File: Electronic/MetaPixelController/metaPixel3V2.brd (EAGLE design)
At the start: 100 x 80 mm, 3 parts, among them IC1 74HC245N

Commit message: fixing include stuff
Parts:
- added JP1: (no value), pinhead:1X01
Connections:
- removed net !MEM_CS: U$1.6
- removed net !SD_CS: U$1.10
- removed net A_BCLK: U$1.9
- removed net A_LRCLK: U$1.23/A9
- removed net A_MCLK: U$1.11
- removed net A_RX: U$1.13
- removed net A_TX: U$1.22/A8
- removed net SCL: U$1.19/A5
- removed net SDA: U$1.18/A4
- net !LCD_CS: now also U$1.10; no longer U$1.20/A6
- net LCD_DC: now also U$1.9; no longer U$1.15/A1
- net LCD_LED: now also JP1.1; no longer U$1.3
- net MOSI: now also U$1.11; no longer U$1.7
- net SCLK: now also U$1.13; no longer U$1.14/A0
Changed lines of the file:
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@@
 </element>
 <element name="U$1" library="Teensy3.0" package="TEENSY_3.0_BASIC" value="TEENSY_3.0_BASIC" x="25.4" y="26.67"/>
+<element name="JP1" library="pinhead" package="1X01" value="" x="2.54" y="-3.81"/>
 </elements>
 <signals>
@@
 </signal>
 <signal name="SCLK">
-<contactref element="U$1" pad="14/A0"/>
 <contactref element="SV1" pad="10"/>
 <wire x1="91.44" y1="28.3464" x2="91.44" y2="29.21" width="0.254" layer="16"/>
@@
 <wire x1="42.9768" y1="22.6314" x2="88.9254" y2="22.6314" width="0.254" layer="16"/>
 <wire x1="33.147" y1="12.8016" x2="42.9768" y2="22.6314" width="0.254" layer="16"/>
-<wire x1="33.147" y1="12.8016" x2="33.02" y2="12.7" width="0.254" layer="16"/>
-</signal>
-<signal name="A_BCLK">
-<contactref element="U$1" pad="9"/>
+<contactref element="U$1" pad="13"/>
+<wire x1="33.02" y1="10.16" x2="33.147" y2="12.8016" width="0" layer="19" extent="16-16"/>
 </signal>
 <signal name="MOSI">
-<contactref element="U$1" pad="7"/>
 <contactref element="SV1" pad="8"/>
 <wire x1="90.297" y1="31.5468" x2="91.44" y2="31.5468" width="0.254" layer="1"/>
@@
 <wire x1="17.8308" y1="22.86" x2="18.9738" y2="24.003" width="0.254" layer="1"/>
 <wire x1="91.44" y1="31.5468" x2="91.44" y2="31.75" width="0.254" layer="1"/>
-<wire x1="17.8308" y1="22.86" x2="17.78" y2="22.86" width="0.254" layer="1"/>
+<contactref element="U$1" pad="11"/>
+<wire x1="17.78" y1="12.7" x2="17.8308" y2="22.86" width="0" layer="19" extent="1-1"/>
 </signal>
 <signal name="MISO">
-<contactref element="U$1" pad="12"/>
 <contactref element="SV1" pad="9"/>
 <wire x1="57.6072" y1="29.0322" x2="88.6968" y2="29.0322" width="0.254" layer="1"/>
@@
 <wire x1="17.8308" y1="10.287" x2="24.003" y2="16.4592" width="0.254" layer="1"/>
 <wire x1="88.6968" y1="29.0322" x2="88.9" y2="29.21" width="0.254" layer="1"/>
-<wire x1="17.8308" y1="10.287" x2="17.78" y2="10.16" width="0.254" layer="1"/>
-</signal>
-<signal name="A_LRCLK">
-<contactref element="U$1" pad="23/A9"/>
-</signal>
-<signal name="A_RX">
-<contactref element="U$1" pad="13"/>
-</signal>
-<signal name="A_TX">
-<contactref element="U$1" pad="22/A8"/>
-</signal>
-<signal name="A_MCLK">
-<contactref element="U$1" pad="11"/>
-</signal>
-<signal name="!SD_CS">
-<contactref element="U$1" pad="10"/>
-</signal>
-<signal name="!MEM_CS">
-<contactref element="U$1" pad="6"/>
-</signal>
-<signal name="SCL">
-<contactref element="U$1" pad="19/A5"/>
-</signal>
-<signal name="SDA">
-<contactref element="U$1" pad="18/A4"/>
+<contactref element="U$1" pad="12"/>
+<wire x1="17.78" y1="10.16" x2="17.8308" y2="10.287" width="0" layer="19" extent="1-1"/>
 </signal>
 <signal name="LCD_LED">
 <contactref element="SV1" pad="5"/>
-<contactref element="U$1" pad="3"/>
 <wire x1="35.8902" y1="34.29" x2="88.9" y2="34.29" width="0.254" layer="1"/>
 <wire x1="33.3756" y1="36.8046" x2="35.8902" y2="34.29" width="0.254" layer="1"/>
@@
 <wire x1="16.6878" y1="34.0614" x2="16.6878" y2="36.1188" width="0.254" layer="1"/>
 <wire x1="17.6022" y1="33.147" x2="16.6878" y2="34.0614" width="0.254" layer="1"/>
-<wire x1="17.6022" y1="33.147" x2="17.78" y2="33.02" width="0.254" layer="1"/>
+<contactref element="JP1" pad="1"/>
+<wire x1="2.54" y1="-3.81" x2="17.6022" y2="33.147" width="0" layer="19" extent="1-1"/>
 </signal>
 <signal name="!LCD_CS">
 <contactref element="SV1" pad="7"/>
-<contactref element="U$1" pad="20/A6"/>
 <wire x1="85.4964" y1="31.5468" x2="88.6968" y2="31.5468" width="0.254" layer="1"/>
 <wire x1="84.8106" y1="30.861" x2="85.4964" y2="31.5468" width="0.254" layer="1"/>
@@
 <wire x1="33.147" y1="28.1178" x2="55.3212" y2="28.1178" width="0.254" layer="1"/>
 <wire x1="88.6968" y1="31.5468" x2="88.9" y2="31.75" width="0.254" layer="1"/>
-<wire x1="33.147" y1="28.1178" x2="33.02" y2="27.94" width="0.254" layer="1"/>
+<contactref element="U$1" pad="10"/>
+<wire x1="17.78" y1="15.24" x2="33.147" y2="28.1178" width="0" layer="19" extent="1-1"/>
 </signal>
 <signal name="!LCD_RST">
@@
 <signal name="LCD_DC">
 <contactref element="SV1" pad="12"/>
-<contactref element="U$1" pad="15/A1"/>
 <wire x1="90.297" y1="26.5176" x2="91.44" y2="26.5176" width="0.254" layer="1"/>
 <wire x1="89.154" y1="25.3746" x2="90.297" y2="26.5176" width="0.254" layer="1"/>
@@
 <wire x1="33.147" y1="15.3162" x2="48.6918" y2="15.3162" width="0.254" layer="1"/>
 <wire x1="91.44" y1="26.5176" x2="91.44" y2="26.67" width="0.254" layer="1"/>
-<wire x1="33.147" y1="15.3162" x2="33.02" y2="15.24" width="0.254" layer="1"/>
+<contactref element="U$1" pad="9"/>
+<wire x1="17.78" y1="17.78" x2="33.147" y2="15.3162" width="0" layer="19" extent="1-1"/>
 </signal>
 <signal name="3.3V">

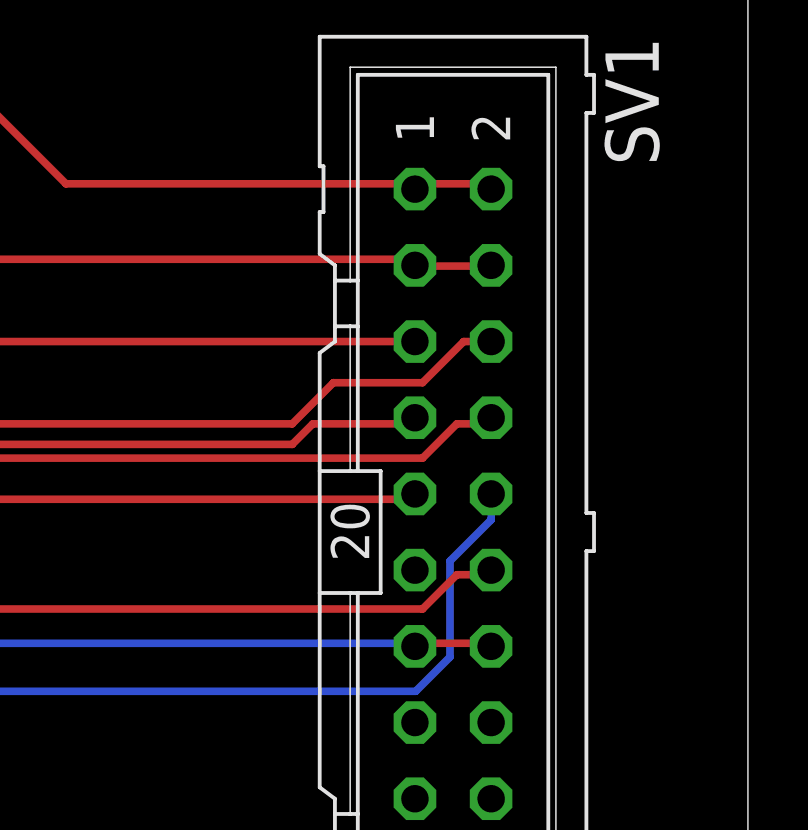
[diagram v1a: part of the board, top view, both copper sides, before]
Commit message: Updated connectors
and more work on the UI Boards
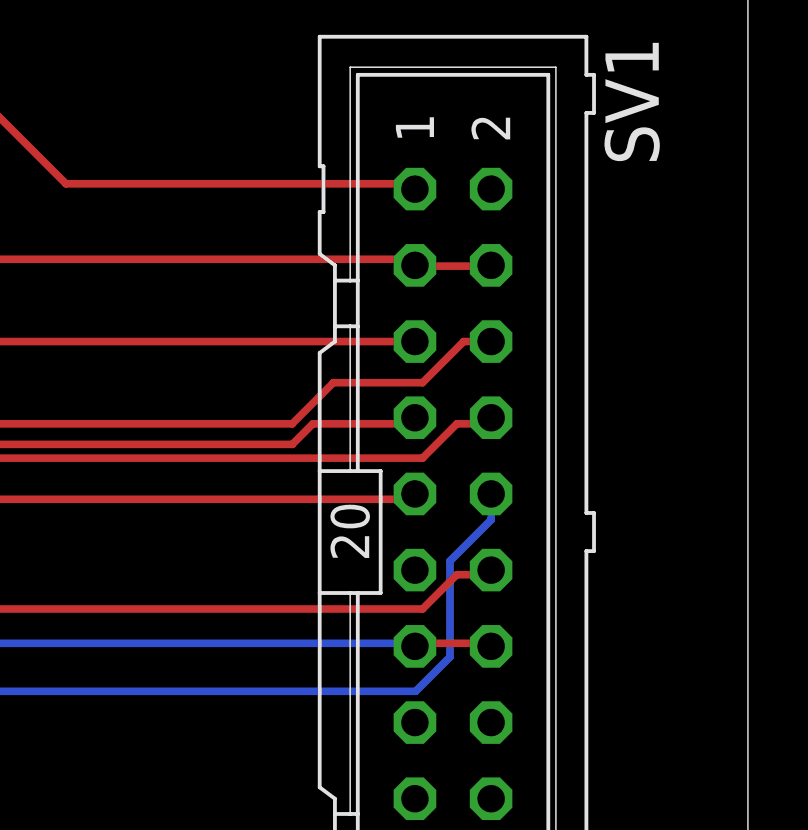
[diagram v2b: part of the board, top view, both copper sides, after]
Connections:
- net 3.3V: no longer SV1.14
- net GND: no longer SV1.2
- net VCC: no longer SV1.4
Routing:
- net GND: track 130.3 -> 127.1 mm
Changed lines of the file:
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@@
 <?xml version="1.0" encoding="utf-8"?>
 <!DOCTYPE eagle SYSTEM "eagle.dtd">
-<eagle version="7.4.0">
+<eagle version="7.4.1">
 <drawing>
 <settings>
@@
 <contactref element="U$1" pad="GND1"/>
 <contactref element="IC1" pad="10"/>
-<contactref element="SV1" pad="1"/>
-<contactref element="SV1" pad="2"/>
 <contactref element="IC1" pad="19"/>
-<wire x1="91.44" y1="39.5478" x2="88.9254" y2="39.5478" width="0.254" layer="1"/>
-<wire x1="88.9254" y1="39.5478" x2="88.9" y2="39.37" width="0.254" layer="1"/>
-<wire x1="91.44" y1="39.5478" x2="91.44" y2="39.37" width="0.254" layer="1"/>
 <wire x1="50.5206" y1="53.721" x2="44.577" y2="59.6646" width="0.254" layer="1"/>
 <wire x1="63.0936" y1="53.721" x2="50.5206" y2="53.721" width="0.254" layer="1"/>
@@
 <wire x1="77.2668" y1="39.5478" x2="88.6968" y2="39.5478" width="0.254" layer="1"/>
 <wire x1="64.9224" y1="51.8922" x2="77.2668" y2="39.5478" width="0.254" layer="1"/>
-<wire x1="88.6968" y1="39.5478" x2="88.9" y2="39.37" width="0.254" layer="1"/>
 <wire x1="64.9224" y1="51.8922" x2="64.77" y2="52.07" width="0.254" layer="1"/>
+<contactref element="SV1" pad="1"/>
+<wire x1="88.6968" y1="39.5478" x2="88.9" y2="39.37" width="0" layer="19" extent="1-1"/>
 </signal>
 <signal name="AGND">
@@
 <contactref element="IC1" pad="1"/>
 <contactref element="SV1" pad="3"/>
-<contactref element="SV1" pad="4"/>
 <wire x1="91.44" y1="36.8046" x2="88.9254" y2="36.8046" width="0.254" layer="1"/>
 <wire x1="88.9254" y1="36.8046" x2="88.9" y2="36.83" width="0.254" layer="1"/>
-<wire x1="91.44" y1="36.8046" x2="91.44" y2="36.83" width="0.254" layer="1"/>
 <wire x1="42.0624" y1="59.6646" x2="42.0624" y2="52.1208" width="0.254" layer="1"/>
 <wire x1="42.0624" y1="52.1208" x2="41.91" y2="52.07" width="0.254" layer="1"/>
@@
 <contactref element="U$1" pad="3.3V1"/>
 <contactref element="SV1" pad="13"/>
-<contactref element="SV1" pad="14"/>
 <wire x1="91.44" y1="24.2316" x2="88.9254" y2="24.2316" width="0.254" layer="1"/>
 <wire x1="88.9254" y1="24.2316" x2="88.9" y2="24.13" width="0.254" layer="1"/>
-<wire x1="91.44" y1="24.2316" x2="91.44" y2="24.13" width="0.254" layer="1"/>
 <wire x1="22.86" y1="27.8892" x2="22.86" y2="10.16" width="0.254" layer="16"/>
 <wire x1="32.9184" y1="37.9476" x2="22.86" y2="27.8892" width="0.254" layer="16"/>

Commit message: The first 3 Boards are ready
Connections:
- removed net N$1: IC1.3
- removed net N$2: IC1.4
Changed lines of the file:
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@@
 <contactref element="IC1" pad="18"/>
-</signal>
-<signal name="N$1">
-<contactref element="IC1" pad="3"/>
-</signal>
-<signal name="N$2">
-<contactref element="IC1" pad="4"/>
 </signal>
 <signal name="LCD_DC">
